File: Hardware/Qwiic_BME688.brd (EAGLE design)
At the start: 25.4 x 25.4 mm, 52 parts, among them J2 QWIIC_RA, J4 QWIIC_RA, U1 BME688LGA

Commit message: Update net names
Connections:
- net SDA renamed SDA/POCI
- new net SDO/PICO: U1.5
- net SDO: no longer U1.5
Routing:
- net SDO: track 14.2 -> 13.3 mm
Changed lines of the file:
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@@
 <drawing>
 <settings>
-<setting alwaysvectorfont="no"/>
+<setting alwaysvectorfont="yes"/>
 <setting keepoldvectorfont="yes"/>
 <setting verticaltext="up"/>
@@
 <layer number="37" name="tTest" color="7" fill="1" visible="no" active="yes"/>
 <layer number="38" name="bTest" color="7" fill="1" visible="no" active="yes"/>
-<layer number="39" name="tKeepout" color="4" fill="11" visible="yes" active="yes"/>
+<layer number="39" name="tKeepout" color="4" fill="11" visible="no" active="yes"/>
 <layer number="40" name="bKeepout" color="1" fill="11" visible="no" active="yes"/>
-<layer number="41" name="tRestrict" color="4" fill="10" visible="yes" active="yes"/>
+<layer number="41" name="tRestrict" color="4" fill="10" visible="no" active="yes"/>
 <layer number="42" name="bRestrict" color="1" fill="10" visible="no" active="yes"/>
 <layer number="43" name="vRestrict" color="2" fill="10" visible="no" active="yes"/>
@@
 <layer number="45" name="Holes" color="7" fill="1" visible="yes" active="yes"/>
 <layer number="46" name="Milling" color="3" fill="1" visible="no" active="yes"/>
-<layer number="47" name="Measures" color="7" fill="1" visible="yes" active="yes"/>
+<layer number="47" name="Measures" color="7" fill="1" visible="no" active="yes"/>
 <layer number="48" name="Document" color="7" fill="1" visible="no" active="yes"/>
 <layer number="49" name="Reference" color="7" fill="1" visible="no" active="yes"/>
@@
 <wire x1="18.669" y1="1.27" x2="16.694" y2="3.245" width="0.2032" layer="1"/>
 </signal>
-<signal name="SDA">
+<signal name="SDA/POCI">
 <contactref element="J2" pad="3"/>
 <contactref element="J4" pad="3"/>
@@
 </signal>
 <signal name="SDO">
-<contactref element="U1" pad="5"/>
 <contactref element="ADR" pad="2"/>
 <contactref element="J3" pad="6"/>
-<wire x1="11.5" y1="11.5" x2="11.5" y2="10.611" width="0.2032" layer="1"/>
 <wire x1="11.5" y1="10.611" x2="11.43" y2="10.541" width="0.2032" layer="1"/>
 <via x="11.43" y="10.541" extent="1-16" drill="0.3048"/>
@@
 <wire x1="8.04" y1="9.232" x2="8.04" y2="10.16" width="0.2032" layer="1"/>
 </signal>
+<signal name="SDO/PICO">
+<contactref element="U1" pad="5"/>
+</signal>
 </signals>

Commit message: Fixed formatting of examples
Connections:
- net SCL renamed SCL/SCK
- net SDA/POCI renamed SDA/PICO
- removed net SDO: ADR.2, J3.6
- removed net SDO/PICO: U1.5
- new net SDO/POCI: ADR.2, J3.6, U1.5
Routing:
- net SDO/POCI: track 0.00 -> 13.3 mm, vias 0 -> 1
- net SDO: track 13.3 -> 0.00 mm, vias 1 -> 0
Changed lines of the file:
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@@
 <drawing>
 <settings>
-<setting alwaysvectorfont="yes"/>
+<setting alwaysvectorfont="no"/>
 <setting keepoldvectorfont="yes"/>
 <setting verticaltext="up"/>
@@
 <via x="12.319" y="11.938" extent="1-16" drill="0.3048"/>
 </signal>
-<signal name="SCL">
+<signal name="SCL/SCK">
 <contactref element="J2" pad="4"/>
 <contactref element="J4" pad="4"/>
@@
 <wire x1="18.669" y1="1.27" x2="16.694" y2="3.245" width="0.2032" layer="1"/>
 </signal>
-<signal name="SDA/POCI">
+<signal name="SDA/PICO">
 <contactref element="J2" pad="3"/>
 <contactref element="J4" pad="3"/>
@@
 <wire x1="16.1036" y1="18.9484" x2="16.1036" y2="20.32" width="0.2032" layer="16"/>
 </signal>
-<signal name="SDO">
-<contactref element="ADR" pad="2"/>
-<contactref element="J3" pad="6"/>
-<wire x1="11.5" y1="10.611" x2="11.43" y2="10.541" width="0.2032" layer="1"/>
-<via x="11.43" y="10.541" extent="1-16" drill="0.3048"/>
-<wire x1="11.43" y1="10.541" x2="11.43" y2="9.398" width="0.2032" layer="16"/>
-<wire x1="11.43" y1="9.398" x2="11.43" y2="5.715" width="0.2032" layer="16"/>
-<wire x1="11.43" y1="5.715" x2="10.414" y2="4.699" width="0.2032" layer="16"/>
-<wire x1="10.414" y1="4.699" x2="7.239" y2="4.699" width="0.2032" layer="16"/>
-<wire x1="7.239" y1="4.699" x2="6.35" y2="3.81" width="0.2032" layer="16"/>
-<wire x1="6.35" y1="3.81" x2="6.35" y2="1.27" width="0.2032" layer="16"/>
-</signal>
 <signal name="CSB">
 <contactref element="U1" pad="2"/>
@@
 <wire x1="8.04" y1="9.232" x2="8.04" y2="10.16" width="0.2032" layer="1"/>
 </signal>
-<signal name="SDO/PICO">
+<signal name="SDO/POCI">
 <contactref element="U1" pad="5"/>
+<contactref element="ADR" pad="2"/>
+<contactref element="J3" pad="6"/>
+<wire x1="11.5" y1="10.611" x2="11.43" y2="10.541" width="0.2032" layer="1"/>
+<via x="11.43" y="10.541" extent="1-16" drill="0.3048"/>
+<wire x1="11.43" y1="10.541" x2="11.43" y2="9.398" width="0.2032" layer="16"/>
+<wire x1="11.43" y1="9.398" x2="11.43" y2="5.715" width="0.2032" layer="16"/>
+<wire x1="11.43" y1="5.715" x2="10.414" y2="4.699" width="0.2032" layer="16"/>
+<wire x1="10.414" y1="4.699" x2="7.239" y2="4.699" width="0.2032" layer="16"/>
+<wire x1="7.239" y1="4.699" x2="6.35" y2="3.81" width="0.2032" layer="16"/>
+<wire x1="6.35" y1="3.81" x2="6.35" y2="1.27" width="0.2032" layer="16"/>
+<wire x1="11.5" y1="10.611" x2="11.5" y2="11.5" width="0" layer="19" extent="1-1"/>
 </signal>
 </signals>

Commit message: Updates to hardware v02
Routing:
- net SDO/POCI: track 13.3 -> 14.2 mm
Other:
- board text added: "v02"
- board text removed: "v01"
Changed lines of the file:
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@@
 <drawing>
 <settings>
-<setting alwaysvectorfont="no"/>
+<setting alwaysvectorfont="yes"/>
 <setting keepoldvectorfont="yes"/>
 <setting verticaltext="up"/>
@@
 <wire x1="25.4" y1="25.4" x2="25.4" y2="0" width="0.2032" layer="20"/>
 <wire x1="25.4" y1="0" x2="0" y2="0" width="0.2032" layer="20"/>
-<text x="1.397" y="19.812" size="1.27" layer="16" font="vector" ratio="15" rot="MR270" align="center">v01</text>
+<text x="1.27" y="19.05" size="1.27" layer="16" font="vector" ratio="15" rot="MR270" align="center">v02</text>
 <dimension x1="0" y1="0" x2="0" y2="25.4" x3="-8.89" y3="12.7" textsize="1.778" textratio="15" layer="47" unit="inch"/>
 <dimension x1="2.54" y1="22.86" x2="2.54" y2="0" x3="-5.08" y3="11.43" textsize="1.778" textratio="15" layer="47" unit="inch"/>
@@
 <contactref element="ADR" pad="2"/>
 <contactref element="J3" pad="6"/>
-<wire x1="11.5" y1="10.611" x2="11.43" y2="10.541" width="0.2032" layer="1"/>
 <via x="11.43" y="10.541" extent="1-16" drill="0.3048"/>
 <wire x1="11.43" y1="10.541" x2="11.43" y2="9.398" width="0.2032" layer="16"/>
@@
 <wire x1="7.239" y1="4.699" x2="6.35" y2="3.81" width="0.2032" layer="16"/>
 <wire x1="6.35" y1="3.81" x2="6.35" y2="1.27" width="0.2032" layer="16"/>
-<wire x1="11.5" y1="10.611" x2="11.5" y2="11.5" width="0" layer="19" extent="1-1"/>
+<wire x1="11.43" y1="10.541" x2="11.5" y2="10.611" width="0.2032" layer="1"/>
+<wire x1="11.5" y1="10.611" x2="11.5" y2="11.5" width="0.2032" layer="1"/>
 </signal>
 </signals>

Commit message: Update version number
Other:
- board text added: "v10"
- board text removed: "v02"
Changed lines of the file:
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@@
 <drawing>
 <settings>
-<setting alwaysvectorfont="yes"/>
+<setting alwaysvectorfont="no"/>
 <setting keepoldvectorfont="yes"/>
 <setting verticaltext="up"/>
@@
 <wire x1="25.4" y1="25.4" x2="25.4" y2="0" width="0.2032" layer="20"/>
 <wire x1="25.4" y1="0" x2="0" y2="0" width="0.2032" layer="20"/>
-<text x="1.27" y="19.05" size="1.27" layer="16" font="vector" ratio="15" rot="MR270" align="center">v02</text>
+<text x="1.27" y="19.05" size="1.27" layer="16" font="vector" ratio="15" rot="MR270" align="center">v10</text>
 <dimension x1="0" y1="0" x2="0" y2="25.4" x3="-8.89" y3="12.7" textsize="1.778" textratio="15" layer="47" unit="inch"/>
 <dimension x1="2.54" y1="22.86" x2="2.54" y2="0" x3="-5.08" y3="11.43" textsize="1.778" textratio="15" layer="47" unit="inch"/>

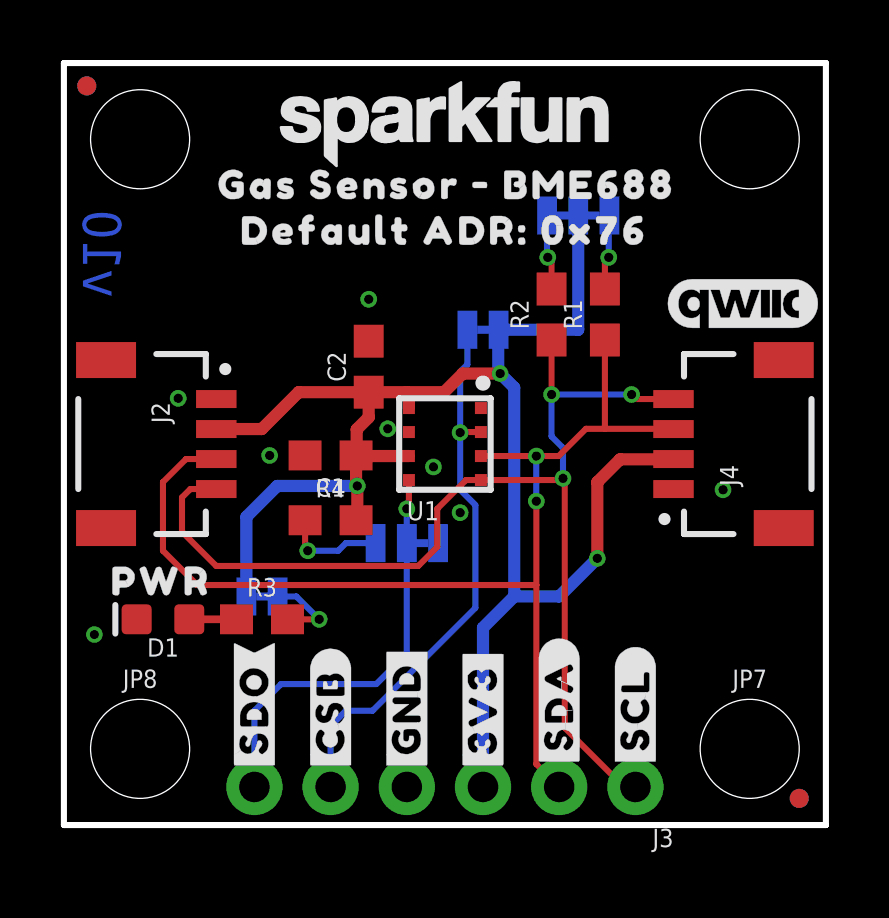
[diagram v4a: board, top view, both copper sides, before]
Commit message: Design review changes
* Add table for jumper selection
* Nudge board name silk (on bottom) to avoid vias
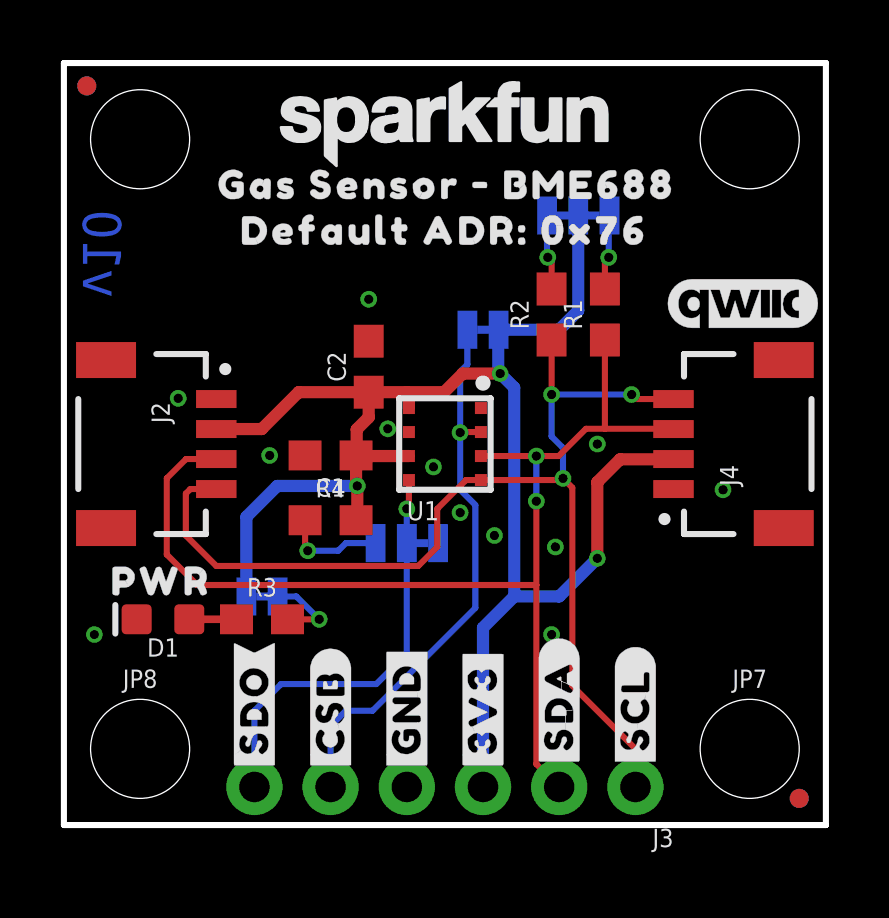
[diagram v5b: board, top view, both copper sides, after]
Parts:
- moved U$7 0.38 mm to (20.3, 13.6)
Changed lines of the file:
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@@
 <drawing>
 <settings>
-<setting alwaysvectorfont="no"/>
+<setting alwaysvectorfont="yes"/>
 <setting keepoldvectorfont="yes"/>
 <setting verticaltext="up"/>
@@
 <element name="U$10" library="output" package="GAS_SENSOR_#_BME6880" value="" x="4.445" y="21.336" smashed="yes"/>
 <element name="U$11" library="output" package="#ADR#0" value="" x="13.589" y="11.176" smashed="yes" rot="MR0"/>
-<element name="U$7" library="output" package="GAS_SENSOR_#_BME6880" value="" x="20.32" y="13.97" smashed="yes" rot="MR0"/>
+<element name="U$7" library="output" package="GAS_SENSOR_#_BME6880" value="" x="20.32" y="13.589" smashed="yes" rot="MR0"/>
 <element name="J3" library="SparkFun-Connectors" package="1X06_NO_SILK" value="" x="19.05" y="1.27" smashed="yes" rot="R180">
 <attribute name="NAME" x="20.32" y="-0.127" size="0.6096" layer="25" font="vector" ratio="20" rot="R180"/>
@@
 <wire x1="17.78" y1="11.43" x2="18.542" y2="12.192" width="0.4064" layer="1"/>
 <wire x1="18.542" y1="12.192" x2="20.328" y2="12.192" width="0.4064" layer="1"/>
-<wire x1="17.145" y1="20.32" x2="17.145" y2="16.51" width="0.4064" layer="16"/>
+<wire x1="17.145" y1="20.32" x2="17.145" y2="17.145" width="0.4064" layer="16"/>
+<wire x1="17.145" y1="17.145" x2="16.51" y2="16.51" width="0.4064" layer="16"/>
 <contactref element="U1" pad="8"/>
 <contactref element="CSB" pad="1"/>
@@
 <wire x1="13.97" y1="1.27" x2="13.97" y2="6.5786" width="0.4064" layer="16"/>
 <wire x1="13.97" y1="6.5786" x2="15.0114" y2="7.62" width="0.4064" layer="16"/>
-<wire x1="17.145" y1="16.51" x2="14.4907" y2="16.51" width="0.4064" layer="16"/>
+<wire x1="16.51" y1="16.51" x2="14.4907" y2="16.51" width="0.4064" layer="16"/>
 <wire x1="14.4907" y1="16.51" x2="14.478" y2="16.51" width="0.4064" layer="16"/>
 <wire x1="15.0114" y1="7.62" x2="15.0114" y2="14.5796" width="0.4064" layer="16"/>
@@
 <contactref element="J3" pad="4"/>
 <via x="12.319" y="11.938" extent="1-16" drill="0.3048"/>
+<via x="14.351" y="9.652" extent="1-16" drill="0.3048"/>
+<via x="16.256" y="6.35" extent="1-16" drill="0.3048"/>
+<via x="17.78" y="12.7" extent="1-16" drill="0.3048"/>
+<via x="16.383" y="9.271" extent="1-16" drill="0.3048"/>
 </signal>
 <signal name="SCL/SCK">
@@
 <contactref element="U1" pad="4"/>
 <wire x1="13.9" y1="11.5" x2="16.694" y2="11.5" width="0.2032" layer="1"/>
+<wire x1="16.948" y1="11.246" x2="16.694" y2="11.5" width="0.2032" layer="1"/>
 <wire x1="16.694" y1="11.5" x2="16.637" y2="11.557" width="0.2032" layer="1"/>
 <via x="16.637" y="11.557" extent="1-16" drill="0.3048"/>
@@
 <via x="16.256" y="14.351" extent="1-16" drill="0.3048"/>
 <wire x1="5.08" y1="11.2" x2="4.215" y2="11.2" width="0.2032" layer="1"/>
-<wire x1="3.937" y1="10.922" x2="3.937" y2="9.779" width="0.2032" layer="1"/>
-<wire x1="3.937" y1="9.779" x2="5.08" y2="8.636" width="0.2032" layer="1"/>
+<wire x1="4.064" y1="11.049" x2="4.064" y2="9.652" width="0.2032" layer="1"/>
+<wire x1="4.064" y1="9.652" x2="5.08" y2="8.636" width="0.2032" layer="1"/>
 <wire x1="11.811" y1="8.636" x2="12.446" y2="9.271" width="0.2032" layer="1"/>
 <wire x1="12.446" y1="9.271" x2="12.446" y2="10.541" width="0.2032" layer="1"/>
 <wire x1="12.446" y1="10.541" x2="13.405" y2="11.5" width="0.2032" layer="1"/>
 <wire x1="13.405" y1="11.5" x2="13.9" y2="11.5" width="0.2032" layer="1"/>
-<wire x1="4.215" y1="11.2" x2="3.937" y2="10.922" width="0.2032" layer="1"/>
+<wire x1="4.215" y1="11.2" x2="4.064" y2="11.049" width="0.2032" layer="1"/>
 <wire x1="5.08" y1="8.636" x2="11.811" y2="8.636" width="0.2032" layer="1"/>
 <contactref element="J3" pad="1"/>
-<wire x1="16.694" y1="3.245" x2="16.694" y2="11.5" width="0.2032" layer="1"/>
-<wire x1="19.05" y1="1.27" x2="18.669" y2="1.27" width="0.2032" layer="1"/>
-<wire x1="18.669" y1="1.27" x2="16.694" y2="3.245" width="0.2032" layer="1"/>
+<wire x1="16.948" y1="4.642" x2="16.948" y2="11.246" width="0.2032" layer="1"/>
+<wire x1="19.05" y1="1.27" x2="19.05" y2="2.54" width="0.2032" layer="1"/>
+<wire x1="19.05" y1="2.54" x2="16.948" y2="4.642" width="0.2032" layer="1"/>
 </signal>
 <signal name="SDA/PICO">
@@
 <via x="15.748" y="12.3" extent="1-16" drill="0.3048"/>
 <wire x1="5.08" y1="12.2" x2="4.072" y2="12.2" width="0.2032" layer="1"/>
-<wire x1="4.072" y1="12.2" x2="3.302" y2="11.43" width="0.2032" layer="1"/>
-<wire x1="3.302" y1="11.43" x2="3.302" y2="9.144" width="0.2032" layer="1"/>
+<wire x1="4.072" y1="12.2" x2="3.429" y2="11.557" width="0.2032" layer="1"/>
+<wire x1="3.429" y1="11.557" x2="3.429" y2="9.017" width="0.2032" layer="1"/>
 <wire x1="4.445" y1="8.001" x2="15.748" y2="8.001" width="0.2032" layer="1"/>
-<wire x1="3.302" y1="9.144" x2="4.445" y2="8.001" width="0.2032" layer="1"/>
+<wire x1="3.429" y1="9.017" x2="4.445" y2="8.001" width="0.2032" layer="1"/>
 <contactref element="J3" pad="2"/>
 <wire x1="16.51" y1="1.27" x2="15.748" y2="2.032" width="0.2032" layer="1"/>

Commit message: Update the CSB label
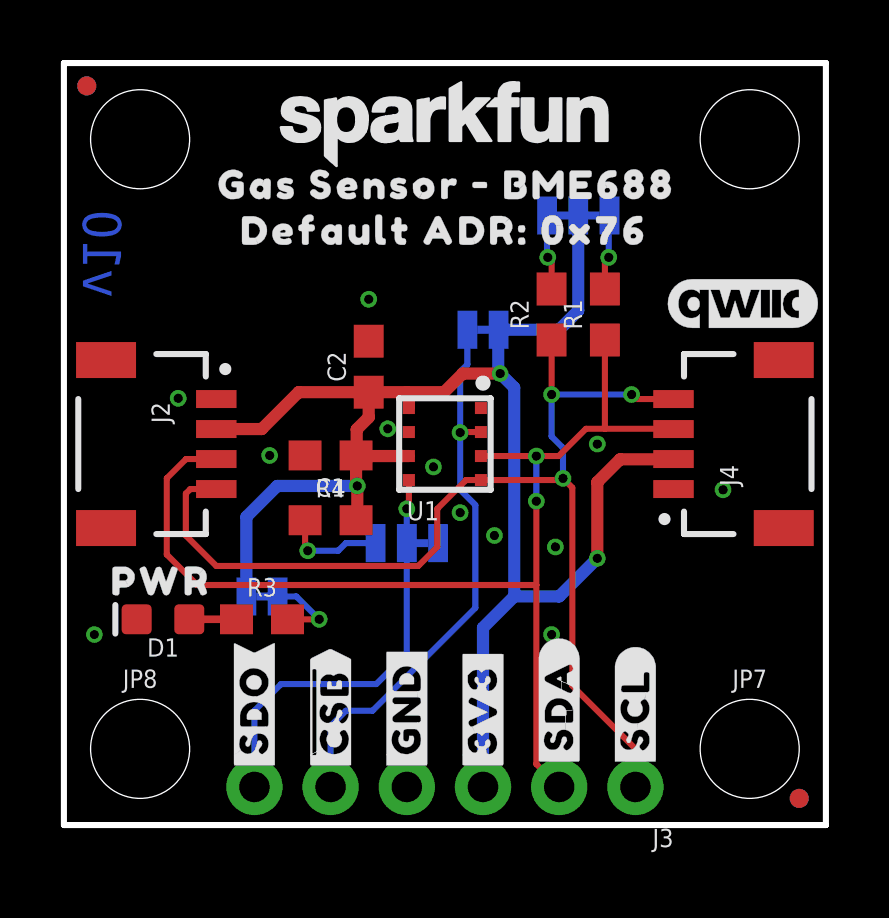
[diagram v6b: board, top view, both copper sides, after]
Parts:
- removed U$17, U$18: (no value), output:#CSB#0
- added U$21, U$22: (no value), output:##CSB##0
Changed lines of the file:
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@@
 <?xml version="1.0" encoding="utf-8"?>
 <!DOCTYPE eagle SYSTEM "eagle.dtd">
-<eagle version="9.5.2">
+<eagle version="9.6.2">
 <drawing>
 <settings>
@@
 <element name="U$2" library="output" package="#SDO#0" value="" x="6.35" y="1.651" smashed="yes" rot="R90"/>
 <element name="U$16" library="output" package="#SDO#0" value="" x="6.35" y="1.651" smashed="yes" rot="MR90"/>
-<element name="U$17" library="output" package="#CSB#0" value="" x="8.89" y="1.651" smashed="yes" rot="R90"/>
-<element name="U$18" library="output" package="#CSB#0" value="" x="8.89" y="1.651" smashed="yes" rot="MR90"/>
 <element name="U$19" library="output" package="#SDI#0" value="" x="16.51" y="1.778" smashed="yes" rot="MR90"/>
 <element name="U$20" library="output" package="#SCK#0" value="" x="19.05" y="1.778" smashed="yes" rot="MR90"/>
 <element name="U$3" library="output" package="#CSB#0" value="" x="13.208" y="16.51" smashed="yes" rot="MR0"/>
+<element name="U$21" library="output" package="##CSB##0" value="" x="8.89" y="1.651" smashed="yes" rot="MR90"/>
+<element name="U$22" library="output" package="##CSB##0" value="" x="8.89" y="1.651" smashed="yes" rot="R90"/>
 </elements>
 <signals>

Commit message: QC Double-check:
* Add active low line to "CSB" net label in the schematic
* Updated jumper selection table
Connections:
- net CSB renamed !CSB!
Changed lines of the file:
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@@
 <?xml version="1.0" encoding="utf-8"?>
 <!DOCTYPE eagle SYSTEM "eagle.dtd">
-<eagle version="9.6.2">
+<eagle version="9.5.2">
 <drawing>
 <settings>
-<setting alwaysvectorfont="yes"/>
+<setting alwaysvectorfont="no"/>
 <setting keepoldvectorfont="yes"/>
 <setting verticaltext="up"/>
@@
 <wire x1="16.1036" y1="18.9484" x2="16.1036" y2="20.32" width="0.2032" layer="16"/>
 </signal>
-<signal name="CSB">
+<signal name="!CSB!">
 <contactref element="U1" pad="2"/>
 <contactref element="CSB" pad="2"/>

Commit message: Rename PICO/POCI net labels to CIPO/COPI
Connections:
- net SDA/PICO renamed SDA/COPI
- net SDO/POCI renamed SDO/CIPO
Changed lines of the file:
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@@
 <wire x1="19.05" y1="2.54" x2="16.948" y2="4.642" width="0.2032" layer="1"/>
 </signal>
-<signal name="SDA/PICO">
+<signal name="SDA/COPI">
 <contactref element="J2" pad="3"/>
 <contactref element="J4" pad="3"/>
@@
 <wire x1="8.04" y1="9.232" x2="8.04" y2="10.16" width="0.2032" layer="1"/>
 </signal>
-<signal name="SDO/POCI">
+<signal name="SDO/CIPO">
 <contactref element="U1" pad="5"/>
 <contactref element="ADR" pad="2"/>
